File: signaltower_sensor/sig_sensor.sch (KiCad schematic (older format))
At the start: 6 parts, among them J1 5051100892_FFC-FPC_in, J2 5051100892_FFC-FPC_out, U1 BH1620FVC

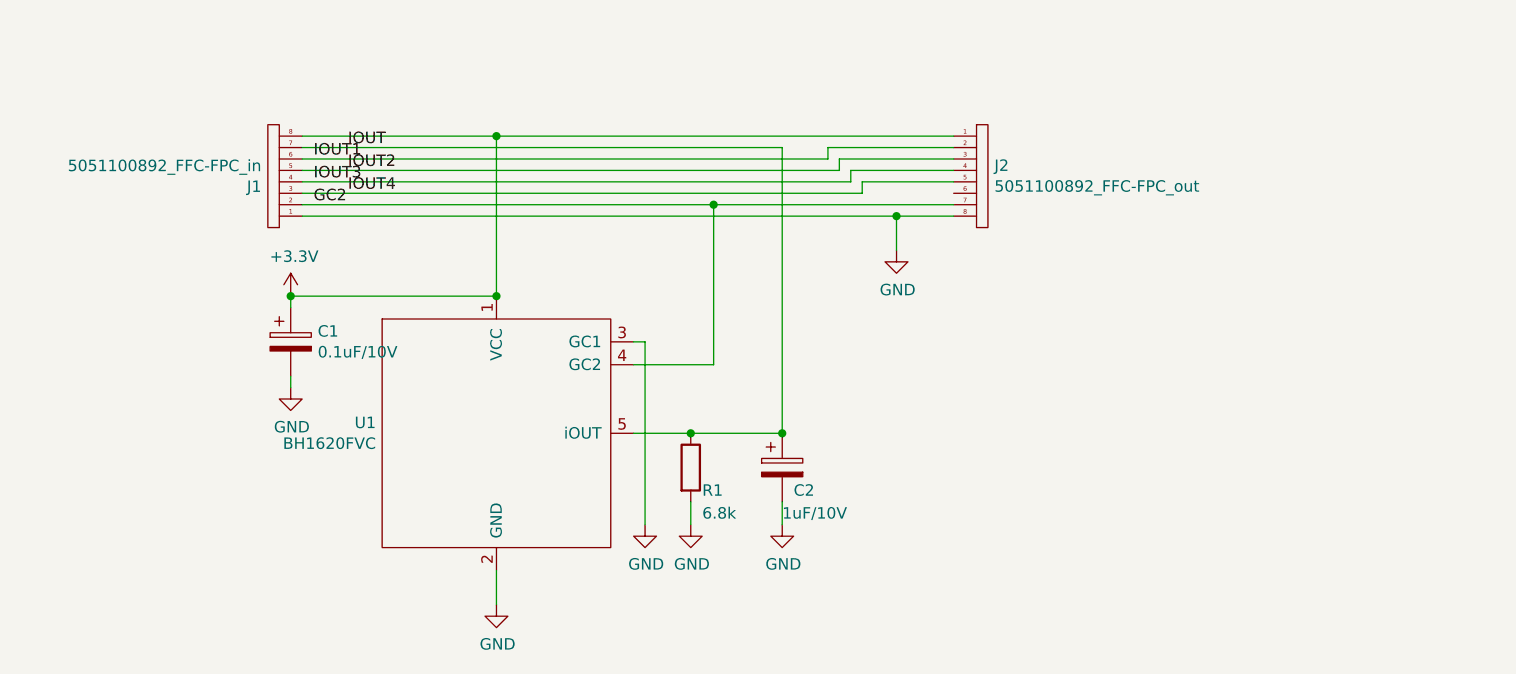
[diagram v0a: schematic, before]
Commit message: update signal sensor host/slave
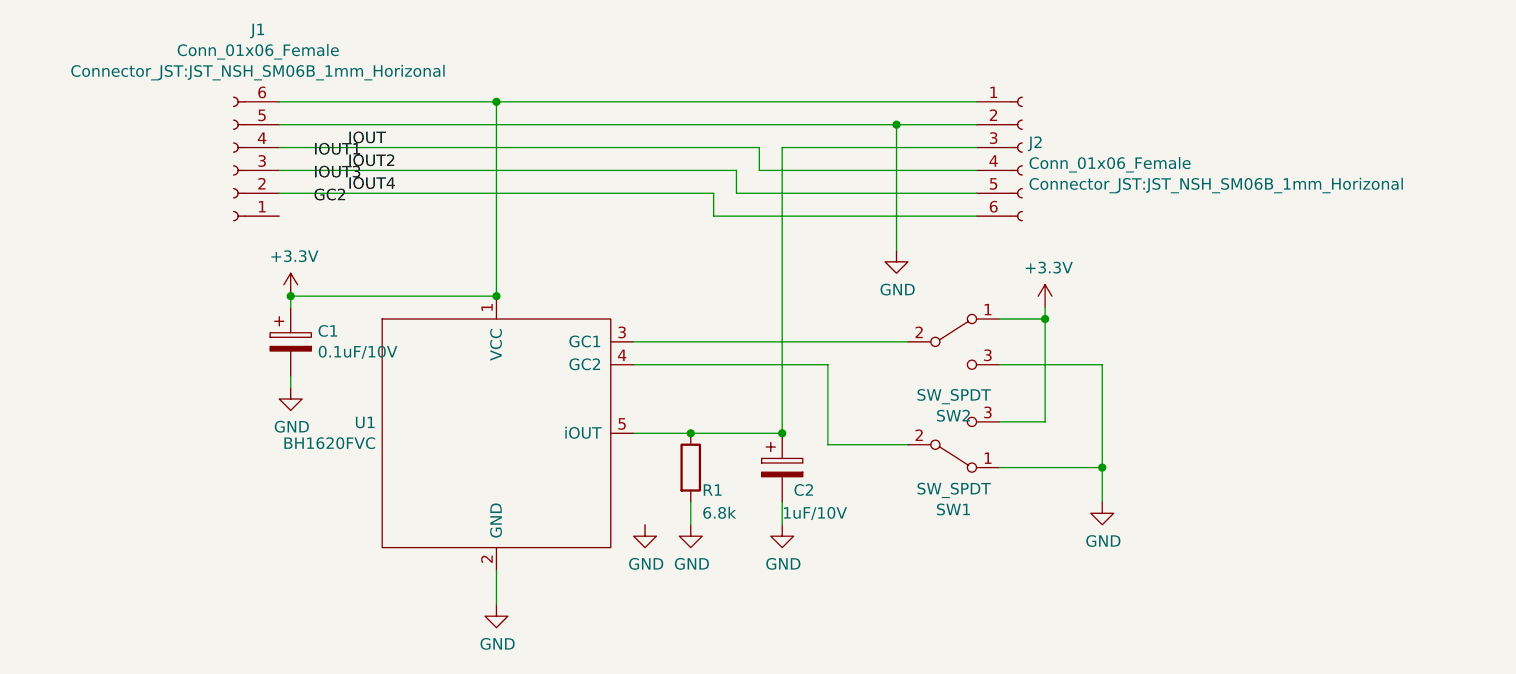
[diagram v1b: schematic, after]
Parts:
- removed J1: 5051100892_FFC-FPC_in, lazurite_footprint:FFC-FPC_5051100892, symbol Other:5051100892_FFC-FPC
- removed J2: 5051100892_FFC-FPC_out, lazurite_footprint:FFC-FPC_5051100892, symbol Other:5051100892_FFC-FPC
- added J1, J2: Conn_01x06_Female, Connector_JST:JST_NSH_SM06B_1mm_Horizonal, symbol Connector:Conn_01x06_Female
- added SW1, SW2: SW_SPDT, lazurite_footprint:SHORT_SPDT, symbol Switch:SW_SPDT
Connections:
- net +3V3: now also J1.6 (Pin_6), J2.1 (Pin_1), SW1.3 (C), SW2.1 (A)
- net GC2: no longer U1.4 (GC2)
- net GND: now also J1.5 (Pin_5), J2.2 (Pin_2), SW1.1 (A), SW2.3 (C); no longer U1.3 (GC1)
- net IOUT: now also J1.4 (Pin_4), J2.4 (Pin_4); no longer C2.1, R1.1, U1.5 (iOUT)
- net IOUT2: now also J1.3 (Pin_3), J2.5 (Pin_5)
- net IOUT4: now also J1.2 (Pin_2), J2.6 (Pin_6)
- new net: SW2.2 (B), U1.3 (GC1)
- new net: SW1.2 (B), U1.4 (GC2)
- new net: C2.1, J2.3 (Pin_3), R1.1, U1.5 (iOUT)
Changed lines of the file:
@@
 	1    0    0    -1
 $EndComp
-Connection ~ 6050 3900
 Wire Wire Line
 	6050 4200 6050 4300
@@
 $EndComp
 Connection ~ 3900 3300
-$Comp
-L Other:5051100892_FFC-FPC J2
-U 1 1 5DBC1B8F
-P 6950 3000
-F 0 "J2" H 6978 3271 50  0000 L CNN
-F 1 "5051100892_FFC-FPC_out" H 6978 3180 50  0000 L CNN
-F 2 "lazurite_footprint:FFC-FPC_5051100892" H 6950 2950 50  0001 C CNN
-F 3 "" H 6950 2950 50  0001 C CNN
-	1    6950 3000
-	1    0    0    -1
-$EndComp
-$Comp
-L Other:5051100892_FFC-FPC J1
-U 1 1 5DBC0D44
-P 3800 2550
-F 0 "J1" H 3828 2821 50  0000 L CNN
-F 1 "5051100892_FFC-FPC_in" H 3828 2730 50  0000 L CNN
-F 2 "lazurite_footprint:FFC-FPC_5051100892" H 3800 2500 50  0001 C CNN
-F 3 "" H 3800 2500 50  0001 C CNN
-	1    3800 2550
-	-1   0    0    1
-$EndComp
-Wire Wire Line
-	3950 2950 6550 2950
-Wire Wire Line
-	3950 2600 4800 2600
-Wire Wire Line
-	3950 2900 5750 2900
-Wire Wire Line
-	6800 2750 6350 2750
-Wire Wire Line
-	6350 2750 6350 2800
-Wire Wire Line
-	6350 2800 3950 2800
-Wire Wire Line
-	6800 2700 6300 2700
-Wire Wire Line
-	6300 2700 6300 2750
-Wire Wire Line
-	6300 2750 3950 2750
-Wire Wire Line
-	6800 2650 6250 2650
-Wire Wire Line
-	6250 2650 6250 2700
-Wire Wire Line
-	6250 2700 3950 2700
 Wire Wire Line
 	3900 3300 4800 3300
@@
 	4800 4500 4800 4650
 Wire Wire Line
-	4800 2600 4800 3300
-Connection ~ 4800 2600
-Wire Wire Line
-	4800 2600 6800 2600
-Connection ~ 4800 3300
-Wire Wire Line
 	5400 3900 5650 3900
 Connection ~ 5650 3900
-Wire Wire Line
-	6050 2650 3950 2650
-Wire Wire Line
-	6050 2650 6050 3900
-Wire Wire Line
-	5750 2900 5750 3600
-Wire Wire Line
-	5750 3600 5400 3600
-Connection ~ 5750 2900
-Wire Wire Line
-	5750 2900 6800 2900
 $Comp
 L power:GND #PWR0106
@@
 	1    0    0    -1
 $EndComp
-Wire Wire Line
-	6550 2950 6550 3100
-Connection ~ 6550 2950
-Wire Wire Line
-	6550 2950 6800 2950
 Text Label 4150 2650 0    50   ~ 0
 IOUT
@@
 Text Label 4000 2800 0    50   ~ 0
 IOUT3
-Wire Wire Line
-	3950 2850 6400 2850
-$Comp
-L power:GND #PWR?
+$Comp
+L power:GND #PWR0107
 U 1 1 5E215390
 P 5450 4300
-F 0 "#PWR?" H 5450 4050 50  0001 C CNN
+F 0 "#PWR0107" H 5450 4050 50  0001 C CNN
 F 1 "GND" H 5455 4127 50  0000 C CNN
 F 2 "" H 5450 4300 50  0001 C CNN
@@
 	1    0    0    -1
 $EndComp
-Wire Wire Line
-	5450 4300 5450 3500
-Wire Wire Line
-	5450 3500 5400 3500
-Wire Wire Line
-	6800 2800 6400 2800
-Wire Wire Line
-	6400 2800 6400 2850
+$Comp
+L Connector:Conn_01x06_Female J1
+U 1 1 5EE04812
+P 3650 2750
+F 0 "J1" H 3542 2135 50  0000 C CNN
+F 1 "Conn_01x06_Female" H 3542 2226 50  0000 C CNN
+F 2 "Connector_JST:JST_NSH_SM06B_1mm_Horizonal" H 3542 2317 50  0000 C CNN
+F 3 "~" H 3650 2750 50  0001 C CNN
+	1    3650 2750
+	-1   0    0    1
+$EndComp
+$Comp
+L Connector:Conn_01x06_Female J2
+U 1 1 5EE06921
+P 7100 2650
+F 0 "J2" H 7128 2671 50  0000 L CNN
+F 1 "Conn_01x06_Female" H 7128 2580 50  0000 L CNN
+F 2 "Connector_JST:JST_NSH_SM06B_1mm_Horizonal" H 7128 2489 50  0000 L CNN
+F 3 "~" H 7100 2650 50  0001 C CNN
+	1    7100 2650
+	1    0    0    -1
+$EndComp
+Wire Wire Line
+	3850 2450 4800 2450
+Wire Wire Line
+	4800 3300 4800 2450
+Connection ~ 4800 3300
+Connection ~ 4800 2450
+Wire Wire Line
+	4800 2450 6900 2450
+Connection ~ 6050 3900
+$Comp
+L power:+3.3V #PWR0109
+U 1 1 5EE3431A
+P 7200 3350
+F 0 "#PWR0109" H 7200 3200 50  0001 C CNN
+F 1 "+3.3V" H 7215 3523 50  0000 C CNN
+F 2 "" H 7200 3350 50  0001 C CNN
+F 3 "" H 7200 3350 50  0001 C CNN
+	1    7200 3350
+	1    0    0    -1
+$EndComp
+Wire Wire Line
+	6250 3950 6250 3600
+Wire Wire Line
+	5400 3600 6250 3600
+Wire Wire Line
+	7000 3400 7200 3400
+Wire Wire Line
+	7200 3400 7200 3350
+Wire Wire Line
+	7000 4050 7450 4050
+Wire Wire Line
+	7450 4050 7450 4200
+Wire Wire Line
+	7000 3850 7200 3850
+Wire Wire Line
+	7200 3850 7200 3400
+Connection ~ 7200 3400
+Wire Wire Line
+	7000 3600 7450 3600
+Wire Wire Line
+	7450 3600 7450 4050
+Connection ~ 7450 4050
+$Comp
+L Switch:SW_SPDT SW1
+U 1 1 5EE92273
+P 6800 3950
+F 0 "SW1" H 6800 4235 50  0000 C CNN
+F 1 "SW_SPDT" H 6800 4144 50  0000 C CNN
+F 2 "lazurite_footprint:SHORT_SPDT" H 6800 3950 50  0001 C CNN
+F 3 "~" H 6800 3950 50  0001 C CNN
+	1    6800 3950
+	1    0    0    1
+$EndComp
+Wire Wire Line
+	6050 2650 6050 3900
+Wire Wire Line
+	3850 2550 6550 2550
+Wire Wire Line
+	6550 3100 6550 2550
+Connection ~ 6550 2550
+Wire Wire Line
+	6550 2550 6900 2550
+Wire Wire Line
+	6900 2650 6050 2650
+Wire Wire Line
+	3850 2650 5950 2650
+Wire Wire Line
+	5950 2650 5950 2750
+Wire Wire Line
+	5950 2750 6900 2750
+Wire Wire Line
+	3850 2750 5850 2750
+Wire Wire Line
+	5850 2750 5850 2850
+Wire Wire Line
+	5850 2850 6900 2850
+Wire Wire Line
+	3850 2850 5750 2850
+Wire Wire Line
+	5750 2850 5750 2950
+Wire Wire Line
+	5750 2950 6900 2950
+Wire Wire Line
+	5400 3500 6600 3500
+Wire Wire Line
+	6250 3950 6600 3950
+$Comp
+L power:GND #PWR0108
+U 1 1 5EFC39E3
+P 7450 4200
+F 0 "#PWR0108" H 7450 3950 50  0001 C CNN
+F 1 "GND" H 7455 4027 50  0000 C CNN
+F 2 "" H 7450 4200 50  0001 C CNN
+F 3 "" H 7450 4200 50  0001 C CNN
+	1    7450 4200
+	1    0    0    -1
+$EndComp
+$Comp
+L Switch:SW_SPDT SW2
+U 1 1 5EE93915
+P 6800 3500
+F 0 "SW2" H 6800 3175 50  0000 C CNN
+F 1 "SW_SPDT" H 6800 3266 50  0000 C CNN
+F 2 "lazurite_footprint:SHORT_SPDT" H 6800 3500 50  0001 C CNN
+F 3 "~" H 6800 3500 50  0001 C CNN
+	1    6800 3500
+	1    0    0    -1
+$EndComp
 $EndSCHEMATC
